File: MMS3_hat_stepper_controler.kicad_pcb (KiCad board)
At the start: 4 copper layers, 100 x 50 mm, 82 parts, among them J1 Chainbus in, J2 Chainbus Out, J3 Conn_01x04_Pin, J4 AMASS XT60 Male, J5 AMASS XT60 Female, J6 Encoder connector, J7 Motor connector, J8 Conn_01x03_Pin, SW1 SW_DIP_x04, U1 SN74CB3Q3384APW, U2 M24C64, U3 TMC5130A-TA, U4 AMS1117, U5 LM2596HVS-ADJRG

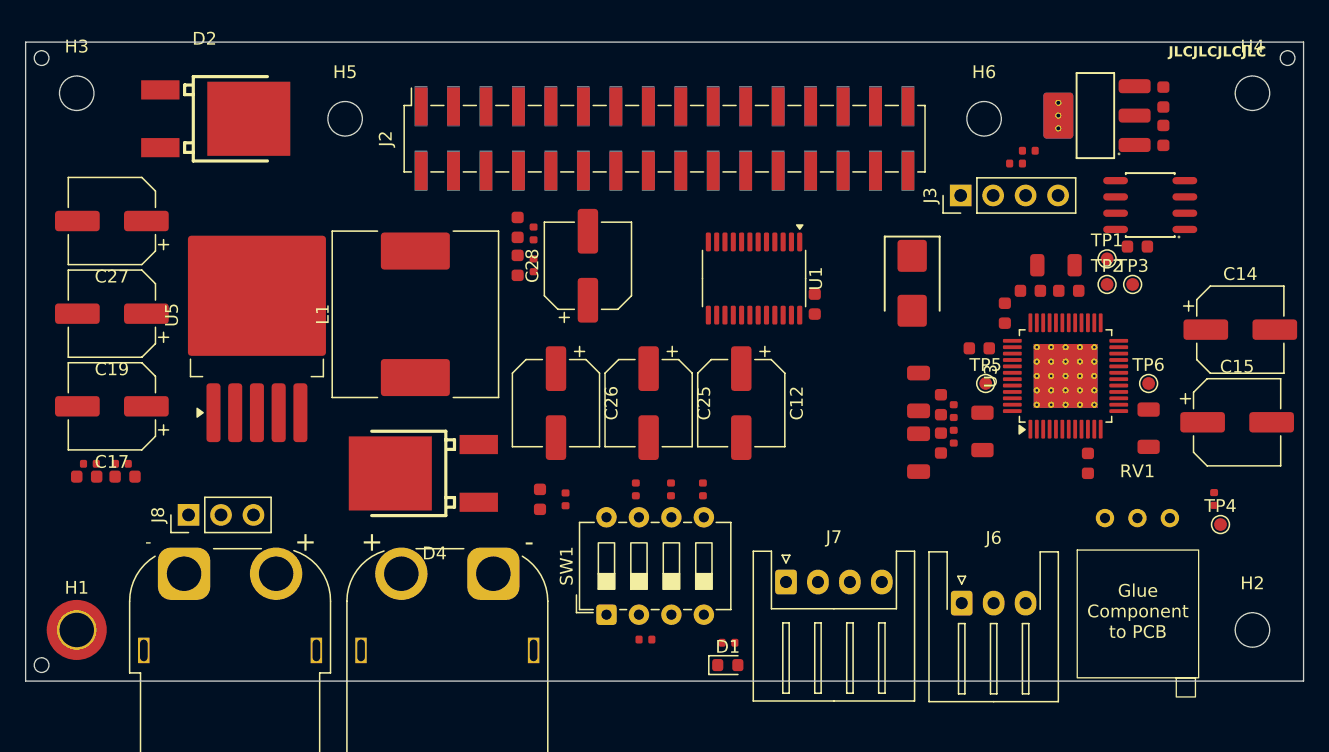
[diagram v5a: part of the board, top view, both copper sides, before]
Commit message: Added Routing
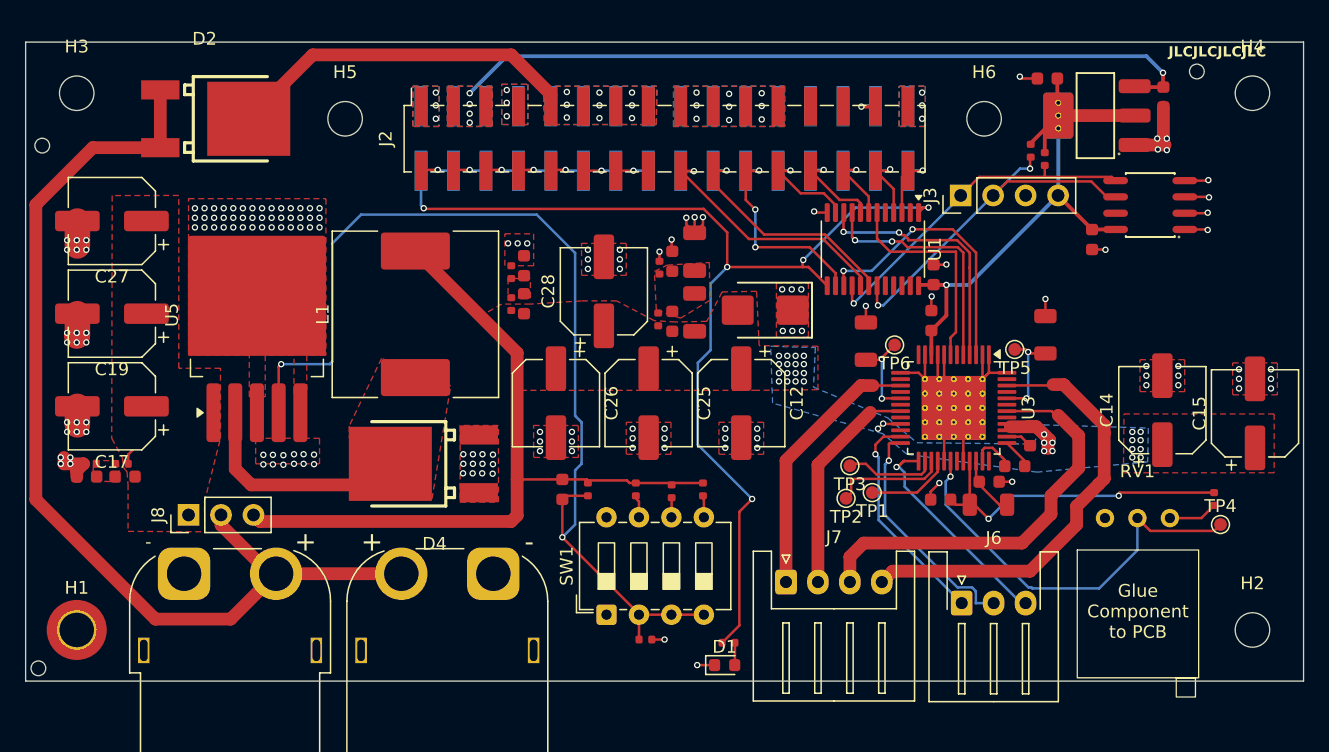
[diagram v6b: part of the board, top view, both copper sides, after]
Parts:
- moved R9 26.6 mm to (127.6, 105.7), turned to 90 degrees
- moved TP2 26.4 mm to (142.2, 123.7), turned to 180 degrees
- moved TP3 26.3 mm to (142.5, 121.2), turned to 180 degrees
- moved TP1 25.9 mm to (144.2, 123.2), turned to 180 degrees
- moved C9 25.4 mm to (128.6, 105.2), turned to 90 degrees
- moved R8 24.2 mm to (127.5, 109.7), turned to 90 degrees
- moved C11 23.5 mm to (130.3, 104.4), turned to 90 degrees
- moved R7 23.2 mm to (143.8, 111.4), turned to 90 degrees
- moved C8 22.0 mm to (128.6, 109.8), turned to 90 degrees
- moved TP6 20.1 mm to (146.0, 111.7), turned to 180 degrees
- moved R4 19.5 mm to (153.3, 124.2), turned to 0 degrees
- moved C4 19.2 mm to (149.6, 123.8), turned to 180 degrees
- moved C10 18.6 mm to (130.3, 109.2), turned to 90 degrees
- moved C3 16.6 mm to (148.9, 109.8), turned to 90 degrees
- moved C6 15.3 mm to (153.4, 122.4), turned to 0 degrees
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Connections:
- J6 pad 1: /Stepper controller/ENCA_DCIN_CFG5 -> /Stepper controller/ENCN_DCO
- J6 pad 3: /Stepper controller/ENCN_DCO -> /Stepper controller/ENCA_DCIN_CFG5
- J7 pad 1: /Stepper controller/OA1 -> /Stepper controller/OB1
- J7 pad 2: /Stepper controller/OA2 -> /Stepper controller/OB2
- J7 pad 3: /Stepper controller/OB1 -> /Stepper controller/OA2
- J7 pad 4: /Stepper controller/OB2 -> /Stepper controller/OA1
- U1 pad 10: unconnected-(U1-1B5-Pad10) -> /Bus_switch/Chainbus.SCK
- U1 pad 11: unconnected-(U1-1A5-Pad11) -> /Bus_switch/Chainbus_In.SCK
- U1 pad 16: /Bus_switch/Chainbus.SCK -> /Bus_switch/Chainbus.SDA
- U1 pad 17: /Bus_switch/Chainbus_In.SCK -> /Bus_switch/Chainbus_In.SDA
- U1 pad 18: /Bus_switch/Chainbus_In.MOSI -> /Bus_switch/Chainbus_In.SCL
- U1 pad 19: /Bus_switch/Chainbus.MOSI -> /Bus_switch/Chainbus.SCL
- U1 pad 2: /Bus_switch/Chainbus.SDA -> /Bus_switch/Chainbus.RX
- U1 pad 20: /Bus_switch/Chainbus.MISO -> unconnected-(U1-2B4-Pad20)
- U1 pad 21: /Bus_switch/Chainbus_In.MISO -> unconnected-(U1-2A4-Pad21)
- U1 pad 3: /Bus_switch/Chainbus_In.SDA -> /Bus_switch/Chainbus_In.RX
- U1 pad 4: /Bus_switch/Chainbus_In.SCL -> /Bus_switch/Chainbus_In.TX
- U1 pad 5: /Bus_switch/Chainbus.SCL -> /Bus_switch/Chainbus.TX
- U1 pad 6: /Bus_switch/Chainbus.TX -> /Bus_switch/Chainbus.MISO
- U1 pad 7: /Bus_switch/Chainbus_In.TX -> /Bus_switch/Chainbus_In.MISO
- U1 pad 8: /Bus_switch/Chainbus_In.RX -> /Bus_switch/Chainbus_In.MOSI
- U1 pad 9: /Bus_switch/Chainbus.RX -> /Bus_switch/Chainbus.MOSI
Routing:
- net /Bus_switch/SEL1: track 0.00 -> 84.8 mm, vias 0 -> 5
- net Net-(U5-FB): track 0.00 -> 82.1 mm, vias 0 -> 2
- net Vin: track 0.00 -> 79.8 mm
- net GND: track 0.00 -> 76.8 mm, vias 0 -> 175
- net U_reg: track 0.00 -> 65.9 mm, vias 0 -> 31
- net +5V: track 0.00 -> 59.4 mm, vias 0 -> 5
- net +3V3: track 0.00 -> 45.0 mm, vias 0 -> 1
- net /Stepper controller/OA1: track 0.00 -> 34.7 mm
- net Net-(U3-AIN_IREF): track 0.00 -> 32.2 mm, vias 0 -> 1
- net /Stepper controller/OA2: track 0.00 -> 32.1 mm
- net /Bus_switch/Chainbus.SCL: track 0.00 -> 29.4 mm, vias 0 -> 2
- net BRD_VIN: track 0.00 -> 27.9 mm, vias 0 -> 9
- net /Bus_switch/Chainbus.SDA: track 0.00 -> 27.1 mm, vias 0 -> 1
- net /Stepper controller/5VOUT: track 0.00 -> 25.8 mm, vias 0 -> 2
- net /Bus_switch/Chainbus.CS: track 0.00 -> 21.7 mm, vias 0 -> 2
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- added copper zone on B.Cu, net +5V
- added copper zone on F.Cu, net +5V
- added copper zone on B.Cu, net BRD_VIN
- added copper zone on F.Cu, net BRD_VIN
- added copper zone on B.Cu, net GND
- added copper zone on F.Cu, net GND
- added copper zone on In1.Cu, net GND
- added copper zone on In2.Cu, net GND
- added copper zone on F.Cu, net Net-(C10-Pad2)
- added copper zone on F.Cu, net Net-(C20-Pad2)
- added copper zone on F.Cu, net Net-(C23-Pad2)
- added copper zone on F.Cu, net Net-(D4-K)
- added copper zone on F.Cu, net Net-(J8-Pin_1)
- added copper zone on B.Cu, net U_reg
- added copper zone on F.Cu, net U_reg

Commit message: updated routing
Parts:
- added JP1: SolderJumper_2_Open, Jumper:SolderJumper-2_P1.3mm_Open_TrianglePad1.0x1.5mm, F.Cu at (128.7, 105.7)
- added JP2: SolderJumper_2_Open, Jumper:SolderJumper-2_P1.3mm_Open_TrianglePad1.0x1.5mm, F.Cu at (128.7, 108.2)
- added JP3: SolderJumper_2_Open, Jumper:SolderJumper-2_P1.3mm_Open_TrianglePad1.0x1.5mm, F.Cu at (128.7, 110.8)
- added TP7: TestPoint, TestPoint:TestPoint_Pad_D1.0mm, F.Cu at (138.6, 115.7)
- added TP8: TestPoint, TestPoint:TestPoint_Pad_D1.0mm, F.Cu at (118.7, 108.4)
- moved D1 55.4 mm to (175.3, 101.4), turned to 90 degrees
- moved R1 52.9 mm to (173.6, 101.1), turned to 90 degrees
- moved H1 42.0 mm to (82.0, 92.0)
- moved H3 42.0 mm to (82.0, 134.0)
- moved C19 28.7 mm to (101.0, 132.9), turned to -90 degrees
- moved C17 28.7 mm to (108.2, 132.9), turned to -90 degrees
- moved J5 28.4 mm to (87.2, 101.4), turned to 90 degrees
- moved J4 27.7 mm to (87.2, 125.6), turned to 90 degrees
- moved C27 26.5 mm to (93.8, 126.9), turned to -90 degrees
- moved J8 17.5 mm to (108.2, 125.8)
- moved C21 15.4 mm to (98.0, 119.4), turned to 0 degrees
- moved R11 14.7 mm to (97.8, 120.4), turned to 0 degrees
- moved R12 12.3 mm to (118.3, 125.6), turned to 0 degrees
- moved R10 9.74 mm to (95.2, 120.4), turned to 0 degrees
- moved C20 9.58 mm to (95.0, 119.4), turned to 0 degrees
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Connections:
- C10 pad 1: U_reg -> /Stepper controller/U_reg_after_jumper
- C12 pad 1: U_reg -> /Stepper controller/U_reg_after_jumper
- C14 pad 1: U_reg -> /Stepper controller/U_reg_after_jumper
- C15 pad 1: U_reg -> /Stepper controller/U_reg_after_jumper
- C7 pad 1: U_reg -> /Stepper controller/U_reg_after_jumper
- C8 pad 1: U_reg -> /Stepper controller/U_reg_after_jumper
- D3 pad 2: U_reg -> /Stepper controller/U_reg_after_jumper
- R8 pad 1: U_reg -> /Stepper controller/U_reg_after_jumper
- U3 pad 21: U_reg -> /Stepper controller/U_reg_after_jumper
- U3 pad 39: U_reg -> /Stepper controller/U_reg_after_jumper
- U3 pad 40: U_reg -> /Stepper controller/U_reg_after_jumper
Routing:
- net U_reg: track 65.9 -> 42.7 mm, vias 31 -> 0
- net Vin: track 79.8 -> 63.8 mm
- net Net-(U5-FB): track 82.1 -> 71.0 mm
- net /Bus_switch/Chainbus.CS: track 21.7 -> 14.2 mm
- net /Bus_switch/SEL1: track 84.8 -> 78.5 mm, vias 5 -> 2
- net /Stepper controller/U_reg_after_jumper: track 0.00 -> 6.16 mm, vias 0 -> 29
- net /Stepper controller/OA2: track 32.1 -> 36.5 mm
- net /Stepper controller/OA1: track 34.7 -> 38.9 mm
- net /Stepper controller/ENCN_DCO: track 17.4 -> 21.1 mm
- net /Stepper controller/OB2: track 17.8 -> 21.2 mm
- net /Stepper controller/OB1: track 20.9 -> 24.3 mm
- net /Bus_switch/Chainbus.SCL: track 29.4 -> 32.6 mm
- net /Bus_switch/Chainbus.SDA: track 27.1 -> 30.3 mm
- net /Stepper controller/ENCA_DCIN_CFG5: track 17.8 -> 20.8 mm
- net Net-(J8-Pin_1): track 1.18 -> 4.05 mm
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- added copper zone on B.Cu, net /Stepper controller/U_reg_after_jumper
- added copper zone on F.Cu, net /Stepper controller/U_reg_after_jumper
- added copper zone on B.Cu, net Vin
- added copper zone on F.Cu, net Vin
- removed copper zone on B.Cu, net U_reg
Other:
- board text added: "DONT change SW1 WITH ON POWER"
- board text added: "SW1 24 9 12 6.2"
- board text added: "Selected"
- board text removed: "3V3"
- board text removed: "5V0"
- board text removed: "B G R C D 3"
- board text removed: "Change DIP on OFF power"
- board text removed: "FW VER. MC1"
- board text removed: "FW VER. MC2"
- board text removed: "G"
- board text removed: "IO R G"
- board text removed: "N/C"
- board text removed: "VIN"

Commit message: minor fixes + production files
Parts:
- added D5: MBRD10100CTTR, SMC_MBRD10100CTTR:TO-252-3_L6.5-W5.8-P4.58-TL, F.Cu at (120.3, 129.5)
- added D6: MBRD10100CTTR, SMC_MBRD10100CTTR:TO-252-3_L6.5-W5.8-P4.58-TL, F.Cu at (128.6, 131.6)
- added D7: MBRD10100CTTR, SMC_MBRD10100CTTR:TO-252-3_L6.5-W5.8-P4.58-TL, F.Cu at (137.8, 131.6)
- added G***: LOGO, Photo:photo, B.Cu at (164.7, 124.5)
- PN1: moved to B.Cu
- moved PN1 96.0 mm to (88.4, 137.2), turned to 180 degrees
- moved SW1 41.5 mm to (92.2, 105.6)
- moved R16 37.8 mm to (102.6, 98.0), turned to -90 degrees
- moved R15 35.3 mm to (103.9, 97.9), turned to -90 degrees
- moved R14 32.9 mm to (105.2, 97.3), turned to -90 degrees
- moved R12 29.6 mm to (103.1, 100.2)
- moved R13 29.2 mm to (105.5, 98.9), turned to 0 degrees
- moved C22 27.1 mm to (105.5, 100.0), turned to 0 degrees
- moved TP4 19.4 mm to (160.8, 109.5)
- moved R5 19.4 mm to (160.7, 107.3)
- moved RV1 16.9 mm to (165.3, 108.5), turned to 90 degrees
- moved C21 13.8 mm to (91.8, 131.8), turned to -90 degrees
- moved R11 13.1 mm to (90.8, 131.5), turned to -90 degrees
- moved TP3 12.5 mm to (153.8, 126.4)
- moved TP1 12.4 mm to (156.7, 123.0)
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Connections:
- J8 pad 3: U_reg -> Net-(J8-Pin_3)
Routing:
- net Net-(U5-FB): track 71.0 -> 38.5 mm, vias 2 -> 1
- net /Stepper controller/5VOUT: track 25.8 -> 51.8 mm
- net U_reg: track 42.7 -> 66.5 mm, vias 0 -> 2
- net Net-(D6-K): track 0.00 -> 14.4 mm
- net Net-(R14-Pad1): track 1.58 -> 13.8 mm, vias 0 -> 1
- net Net-(U3-AIN_IREF): track 32.2 -> 44.0 mm
- net Net-(D5-K): track 0.00 -> 11.4 mm
- net /Stepper controller/OA2: track 36.5 -> 25.5 mm
- net Net-(J8-Pin_3): track 0.00 -> 8.36 mm
- net /Stepper controller/ENCN_DCO: track 21.1 -> 29.4 mm
- net /Stepper controller/ENCA_DCIN_CFG5: track 20.8 -> 28.3 mm
- net /Stepper controller/ENCB_DCEN_CFG4: track 20.6 -> 27.8 mm
- net Net-(R15-Pad1): track 1.59 -> 8.34 mm
- net Net-(D4-K): track 15.3 -> 21.4 mm
- net GND: track 77.0 -> 71.6 mm, vias 163 -> 181
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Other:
- board text added: "All mounting holes Are M2.5"
- board text added: "DONT change SW1 WITH POWER ON"
- board text removed: "CHAINBUS"
- board text removed: "DONT change SW1 WITH ON POWER"
- board text removed: "Encloshure is supposed to have 2mm walls :)"
- board text removed: "Master link"
- board text removed: "USB2.0"
- board text removed: "Ymin LKME5001J102MF"
